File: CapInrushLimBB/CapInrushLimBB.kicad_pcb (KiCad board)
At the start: 2 copper layers, 56.5 x 34.9 mm, 30 parts, among them J1 Screw_Terminal_01x02, J2 Screw_Terminal_01x02, K1 G5LE-1A, Q1 MPSA42, Q2 IRF9540N, Q3 TIP41C, Q4 BSP230 300V 0.21A

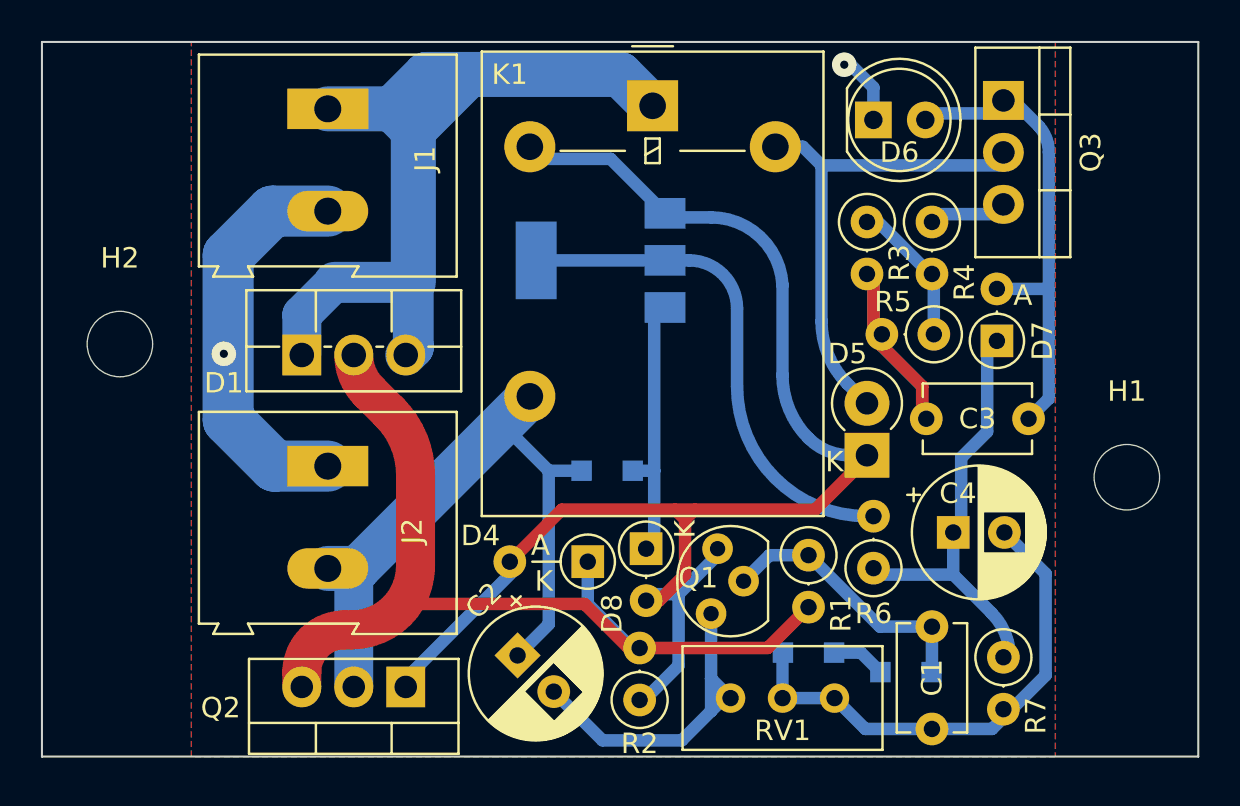
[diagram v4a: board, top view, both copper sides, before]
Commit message: Updated layout and rounded tracks version.
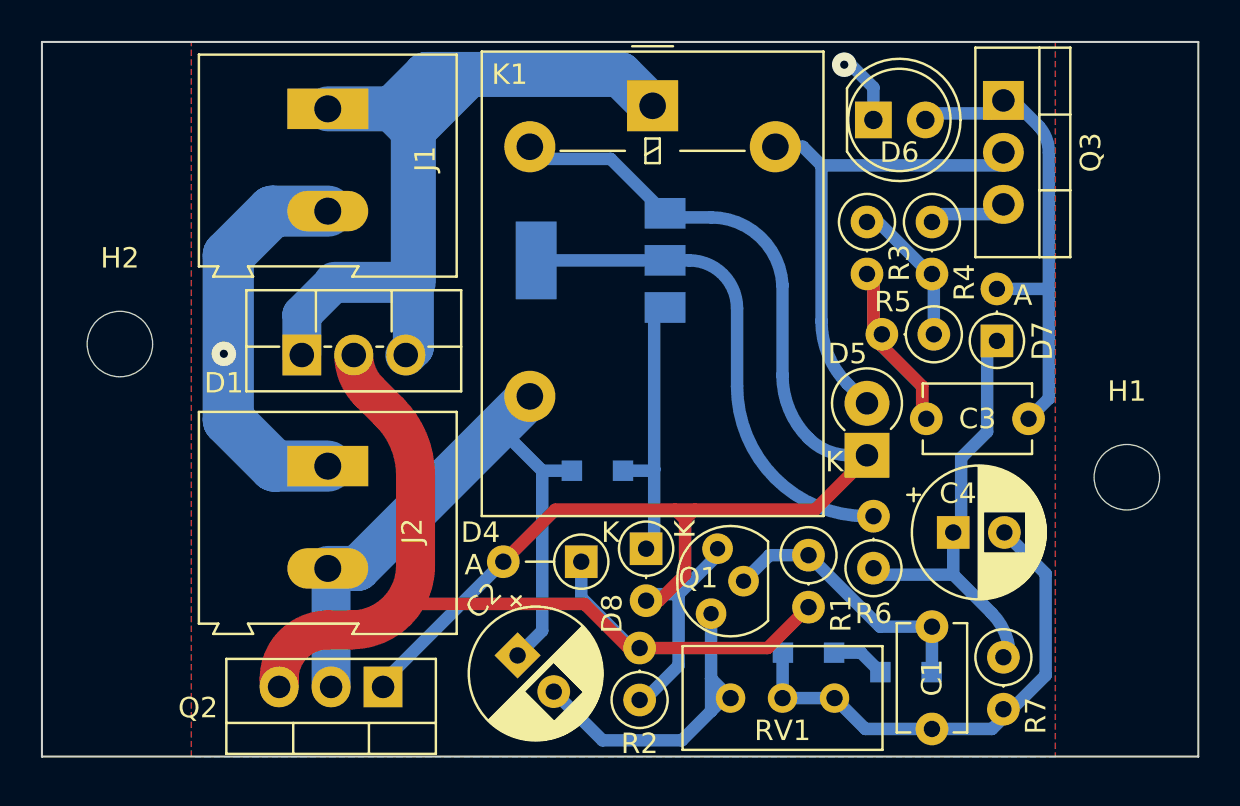
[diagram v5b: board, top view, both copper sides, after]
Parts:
- moved Q2 1.11 mm to (223.7, 156.9)
- moved D9 0.47 mm to (234.2, 146.4)
- moved D4 0.32 mm to (233.4, 150.8)
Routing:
- net /PolProtect: track 47.2 -> 48.3 mm
- net /RLCoilHigh: track 71.0 -> 71.9 mm
- net /RL_Output: track 33.4 -> 32.8 mm
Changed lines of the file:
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@@
   )
   (footprint "Diode_THT:D_DO-35_SOD27_P3.81mm_Vertical_AnodeUp" (layer "F.Cu")
-    (at 233.68613 150.8125 180)
+    (at 233.36863 150.8125 180)
     (descr "Diode, DO-35_SOD27 series, Axial, Vertical, pin pitch=3.81mm, , length*diameter=4*2mm^2, , http://www.diodes.com/_files/packages/DO-35.pdf")
     (tags "Diode DO-35_SOD27 series Axial Vertical pin pitch 3.81mm  length 4mm diameter 2mm")
@@
     (property "Sheetname" "")
     (attr through_hole)
-    (fp_text reference "D4" (at 5.241815 1.27 180) (layer "F.SilkS")
+    (fp_text reference "D4" (at 4.924315 1.42875 180) (layer "F.SilkS")
       (effects (font (size 1 1) (thickness 0.15)))
     )
@@
       (effects (font (size 1 1) (thickness 0.15)))
     )
-    (fp_text user "K" (at 2.144657 -0.9525) (layer "F.SilkS")
-      (effects (font (size 1 1) (thickness 0.15)))
-    )
-    (fp_text user "A" (at 2.31 0.8 180) (layer "F.SilkS")
+    (fp_text user "K" (at -1.425685 1.42875) (layer "F.SilkS")
+      (effects (font (size 1 1) (thickness 0.15)))
+    )
+    (fp_text user "A" (at 5.241815 -0.15875 180) (layer "F.SilkS")
       (effects (font (size 1 1) (thickness 0.15)))
     )
@@
   )
   (footprint "Package_TO_SOT_THT:TO-220-3_Vertical" (layer "F.Cu")
-    (at 224.79 156.9339 180)
+    (at 223.681815 156.9339 180)
     (descr "TO-220-3, Vertical, RM 2.54mm, see https://www.vishay.com/docs/66542/to-220-1.pdf")
     (tags "TO-220-3 Vertical RM 2.54mm")
@@
   )
   (footprint "Diode_SMD:D_SOD-323_HandSoldering" (layer "B.Cu")
-    (at 234.6325 146.3675 180)
+    (at 234.159315 146.3675 180)
     (descr "SOD-323")
     (tags "SOD-323")
@@
   )
   (gr_rect (start 207.01 125.41125) (end 263.525 160.3375) (layer "Edge.Cuts") (width 0.1) (fill none))
-  (segment (start 230.256117 155.394733) (end 231.778065 153.872785) (width 0.6096) (layer "B.Cu") (net 1))
-  (segment (start 231.778065 146.3675) (end 229.555565 144.145) (width 0.6096) (layer "B.Cu") (net 1))
+  (segment (start 221.141815 156.9339) (end 221.141815 151.13) (width 1.905) (layer "B.Cu") (net 1))
   (segment (start 222.445 151.1425) (end 230.855 142.7325) (width 2.2) (layer "B.Cu") (net 1))
-  (segment (start 231.778065 146.3675) (end 233.3825 146.3675) (width 0.6096) (layer "B.Cu") (net 1))
-  (segment (start 231.778065 153.872785) (end 231.778065 146.3675) (width 0.6096) (layer "B.Cu") (net 1))
+  (segment (start 230.256117 155.394733) (end 231.460565 154.190285) (width 0.6096) (layer "B.Cu") (net 1))
   (segment (start 220.98 151.1425) (end 222.445 151.1425) (width 2.2) (layer "B.Cu") (net 1))
-  (segment (start 222.25 156.9339) (end 222.25 151.3375) (width 1.905) (layer "B.Cu") (net 1))
+  (segment (start 232.909315 146.3675) (end 231.460565 146.3675) (width 0.6096) (layer "B.Cu") (net 1))
+  (segment (start 231.460565 146.3675) (end 229.555565 144.4625) (width 0.6096) (layer "B.Cu") (net 1))
+  (segment (start 231.460565 154.190285) (end 231.460565 146.3675) (width 0.6096) (layer "B.Cu") (net 1))
   (segment (start 247.9675 153.9875) (end 244.475 150.495) (width 0.6096) (layer "B.Cu") (net 2))
   (segment (start 250.5075 153.9875) (end 250.5075 156.19) (width 0.6096) (layer "B.Cu") (net 2))
@@
   (segment (start 236.5375 152.7175) (end 237.1725 152.7175) (width 0.6096) (layer "F.Cu") (net 7))
   (segment (start 238.91875 148.2725) (end 238.4425 148.74875) (width 0.6096) (layer "F.Cu") (net 7))
-  (segment (start 237.96086 148.2725) (end 232.41613 148.2725) (width 0.6096) (layer "F.Cu") (net 7))
   (segment (start 237.96086 148.2725) (end 238.91875 148.2725) (width 0.6096) (layer "F.Cu") (net 7))
   (segment (start 244.7925 148.2725) (end 247.3325 145.7325) (width 0.6096) (layer "F.Cu") (net 7))
-  (segment (start 232.41613 148.2725) (end 229.87613 150.8125) (width 0.6096) (layer "F.Cu") (net 7))
   (segment (start 238.4425 151.4475) (end 238.4425 148.74875) (width 0.6096) (layer "F.Cu") (net 7))
   (segment (start 238.91875 148.2725) (end 244.7925 148.2725) (width 0.6096) (layer "F.Cu") (net 7))
+  (segment (start 232.09863 148.2725) (end 229.55863 150.8125) (width 0.6096) (layer "F.Cu") (net 7))
   (segment (start 237.1725 152.7175) (end 238.4425 151.4475) (width 0.6096) (layer "F.Cu") (net 7))
   (segment (start 238.4425 148.74875) (end 237.96086 148.2725) (width 0.6096) (layer "F.Cu") (net 7))
+  (segment (start 237.96086 148.2725) (end 232.09863 148.2725) (width 0.6096) (layer "F.Cu") (net 7))
   (segment (start 236.5375 157.7975) (end 236.22 157.7975) (width 0.6096) (layer "B.Cu") (net 7))
   (segment (start 237.465 133.7875) (end 234.805 131.1275) (width 0.6096) (layer "B.Cu") (net 7))
@@
   (segment (start 246.486604 145.613234) (end 247.3325 145.613234) (width 0.6096) (layer "B.Cu") (net 7))
   (segment (start 237.465 133.7875) (end 237.6625 133.985) (width 0.6096) (layer "B.Cu") (net 7))
-  (segment (start 224.79 156.9339) (end 224.79 156.530565) (width 0.6096) (layer "B.Cu") (net 7))
+  (segment (start 223.681815 156.689315) (end 229.55863 150.8125) (width 0.6096) (layer "B.Cu") (net 7))
   (segment (start 236.445 157.5725) (end 236.22 157.5725) (width 0.6096) (layer "B.Cu") (net 7))
   (segment (start 238.125 152.4) (end 238.125 155.8925) (width 0.6096) (layer "B.Cu") (net 7))
   (segment (start 236.699315 152.7175) (end 237.016815 152.4) (width 0.6096) (layer "B.Cu") (net 7))
+  (segment (start 223.681815 156.9339) (end 223.681815 156.689315) (width 0.6096) (layer "B.Cu") (net 7))
   (segment (start 236.5375 152.7175) (end 236.699315 152.7175) (width 0.6096) (layer "B.Cu") (net 7))
-  (segment (start 224.79 156.530565) (end 230.190565 151.13) (width 0.6096) (layer "B.Cu") (net 7))
   (segment (start 238.125 155.8925) (end 236.445 157.5725) (width 0.6096) (layer "B.Cu") (net 7))
   (segment (start 243.202816 137.29458) (end 243.202816 141.708677) (width 0.6096) (layer "B.Cu") (net 7))
@@
   (segment (start 254 158.4325) (end 254 158.0225) (width 0.6096) (layer "B.Cu") (net 12))
   (segment (start 236.22 155.0325) (end 235.680565 155.0325) (width 0.6096) (layer "F.Cu") (net 13))
-  (segment (start 222.14879 154.14625) (end 221.776815 154.14625) (width 1.905) (layer "F.Cu") (net 13))
-  (segment (start 219.71 156.9339) (end 219.71 156.213065) (width 1.905) (layer "F.Cu") (net 13))
   (segment (start 233.524315 152.87625) (end 224.793065 152.87625) (width 0.6096) (layer "F.Cu") (net 13))
+  (segment (start 225.269315 146.576051) (end 225.269315 151.025725) (width 1.905) (layer "F.Cu") (net 13))
   (segment (start 242.4775 155.0325) (end 244.475 153.035) (width 0.6096) (layer "F.Cu") (net 13))
+  (segment (start 222.991179 142.501863) (end 223.999315 143.51) (width 1.905) (layer "F.Cu") (net 13))
   (segment (start 235.680565 155.0325) (end 233.524315 152.87625) (width 0.6096) (layer "F.Cu") (net 13))
-  (segment (start 225.269315 151.025725) (end 225.269315 146.576051) (width 1.905) (layer "F.Cu") (net 13))
-  (segment (start 222.991179 142.501863) (end 223.999315 143.51) (width 1.905) (layer "F.Cu") (net 13))
+  (segment (start 222.14879 154.14625) (end 220.983065 154.14625) (width 1.905) (layer "F.Cu") (net 13))
   (segment (start 242.4775 155.0325) (end 236.22 155.0325) (width 0.6096) (layer "F.Cu") (net 13))
-  (arc (start 222.14879 154.14625) (mid 224.355334 153.232269) (end 225.269315 151.025725) (width 1.905) (layer "F.Cu") (net 13))
+  (segment (start 218.601815 156.9339) (end 218.601815 156.5275) (width 1.905) (layer "F.Cu") (net 13))
+  (arc (start 222.25 140.7125) (mid 222.442626 141.680896) (end 222.991179 142.501863) (width 1.905) (layer "F.Cu") (net 13))
+  (arc (start 225.269315 151.025725) (mid 224.355334 153.232269) (end 222.14879 154.14625) (width 1.905) (layer "F.Cu") (net 13))
   (arc (start 223.999315 143.51) (mid 224.939253 144.916716) (end 225.269315 146.576051) (width 1.905) (layer "F.Cu") (net 13))
-  (arc (start 222.25 140.7125) (mid 222.442626 141.680896) (end 222.991179 142.501863) (width 1.905) (layer "F.Cu") (net 13))
-  (arc (start 221.776815 154.14625) (mid 220.315356 154.751606) (end 219.71 156.213065) (width 1.905) (layer "F.Cu") (net 13))
-  (segment (start 235.839315 155.0325) (end 233.68613 152.879315) (width 0.6096) (layer "B.Cu") (net 13))
-  (segment (start 233.68613 152.879315) (end 233.68613 150.8125) (width 0.6096) (layer "B.Cu") (net 13))
+  (arc (start 220.983065 154.14625) (mid 219.299267 154.843702) (end 218.601815 156.5275) (width 1.905) (layer "F.Cu") (net 13))
+  (segment (start 233.36863 152.561815) (end 233.36863 150.8125) (width 0.6096) (layer "B.Cu") (net 13))
+  (segment (start 235.839315 155.0325) (end 233.36863 152.561815) (width 0.6096) (layer "B.Cu") (net 13))
   (segment (start 236.22 155.0325) (end 235.839315 155.0325) (width 0.6096) (layer "B.Cu") (net 13))
-  (segment (start 235.8625 146.3675) (end 236.932842 146.3675) (width 0.6096) (layer "B.Cu") (net 14))
-  (segment (start 236.932842 146.3675) (end 236.932842 149.782158) (width 0.6096) (layer "B.Cu") (net 14))
-  (segment (start 236.932842 149.782158) (end 236.5375 150.1775) (width 0.6096) (layer "B.Cu") (net 14))
-  (segment (start 236.932842 146.3675) (end 236.932842 138.3875) (width 0.6096) (layer "B.Cu") (net 14))
+  (segment (start 236.932842 146.292723) (end 236.932842 138.3875) (width 0.6096) (layer "B.Cu") (net 14))
+  (segment (start 236.5375 150.1775) (end 236.932842 149.782158) (width 0.6096) (layer "B.Cu") (net 14))
+  (segment (start 235.409315 146.3675) (end 236.858065 146.3675) (width 0.6096) (layer "B.Cu") (net 14))
+  (segment (start 236.858065 146.3675) (end 236.932842 146.292723) (width 0.6096) (layer "B.Cu") (net 14))
+  (segment (start 236.932842 149.782158) (end 236.932842 146.292723) (width 0.6096) (layer "B.Cu") (net 14))
   (segment (start 250.6 136.8425) (end 250.5075 136.75) (width 0.6096) (layer "B.Cu") (net 15))
   (segment (start 250.6 139.7) (end 250.6 136.8425) (width 0.6096) (layer "B.Cu") (net 15))

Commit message: Changed the reference type, changed current set resistor strategy and updated PCB.
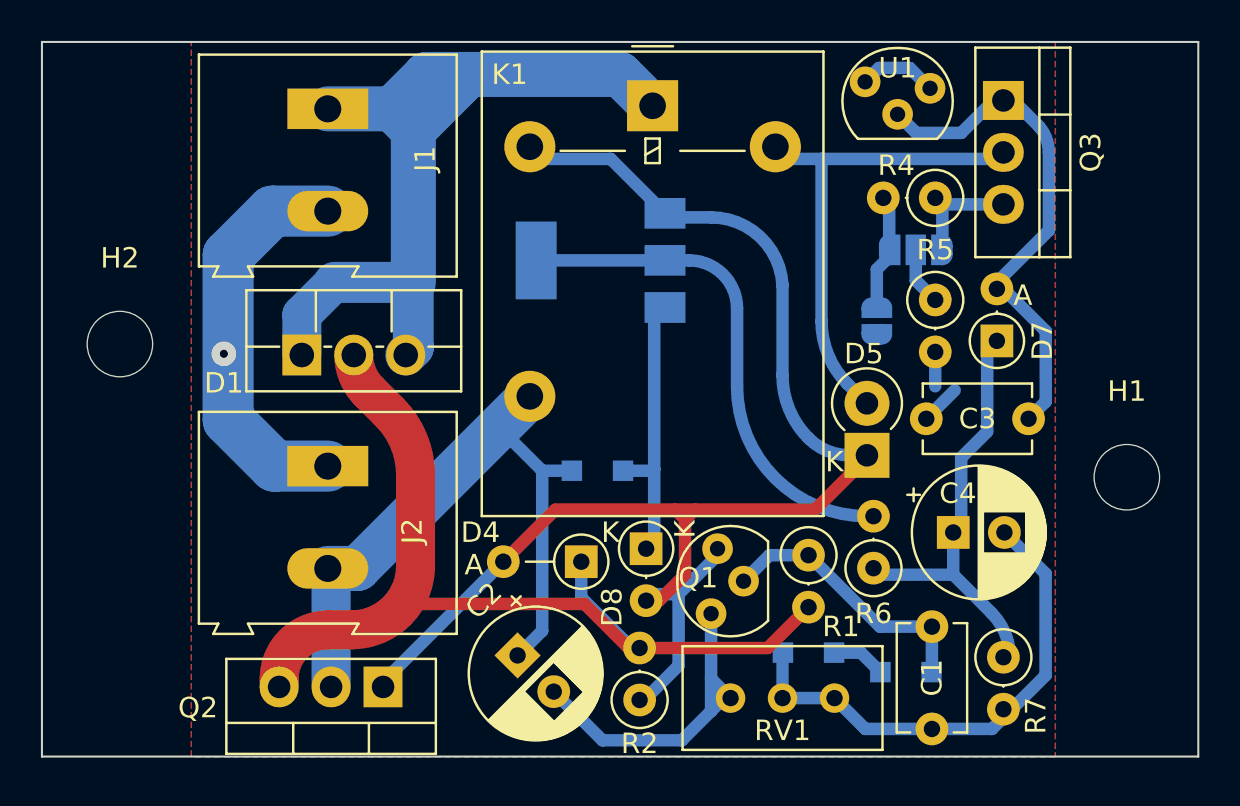
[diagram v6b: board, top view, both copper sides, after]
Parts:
- removed D6: Red LED, LED_THT:LED_D5.0mm
- removed R3: 220R, Resistor_THT:R_Axial_DIN0207_L6.3mm_D2.5mm_P2.54mm_Vertical
- added JP1: SolderJumper_3_Open, Jumper:SolderJumper-3_P1.3mm_Open_RoundedPad1.0x1.5mm, B.Cu at (249.7, 135.6)
- added JP2: SolderJumper_2_Open, Jumper:SolderJumper-2_P1.3mm_Open_RoundedPad1.0x1.5mm, B.Cu at (247.8, 139.1)
- added U1: LM385Z-ADJ, CapInrushLim:TO-92_Inline, F.Cu at (247.6, 128.3)
- R4: value 0R -> 47
- R5: value 110R -> 47
- moved R5 1.68 mm to (250.7, 138.0), turned to -90 degrees
- moved R4 1.19 mm to (250.7, 133.0), turned to 180 degrees
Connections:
- R4 pad 2: Net-(R3-Pad1) -> Net-(JP1-Pad1)
- R5 pad 1: Net-(R3-Pad1) -> Net-(JP1-Pad2)
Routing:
- net /Gnd: track 63.4 -> 52.0 mm, vias 2 -> 1
- net Net-(R3-Pad1): track 6.99 -> 0.00 mm
- net Net-(JP1-Pad1): track 0.00 -> 5.32 mm
- net Net-(JP1-Pad2): track 0.00 -> 2.84 mm
- net Net-(JP1-Pad3): track 3.50 -> 6.15 mm
- net Net-(C3-Pad2): track 22.7 -> 24.6 mm

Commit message: Relayed out relay timer/regulator section to reduce track lengths.
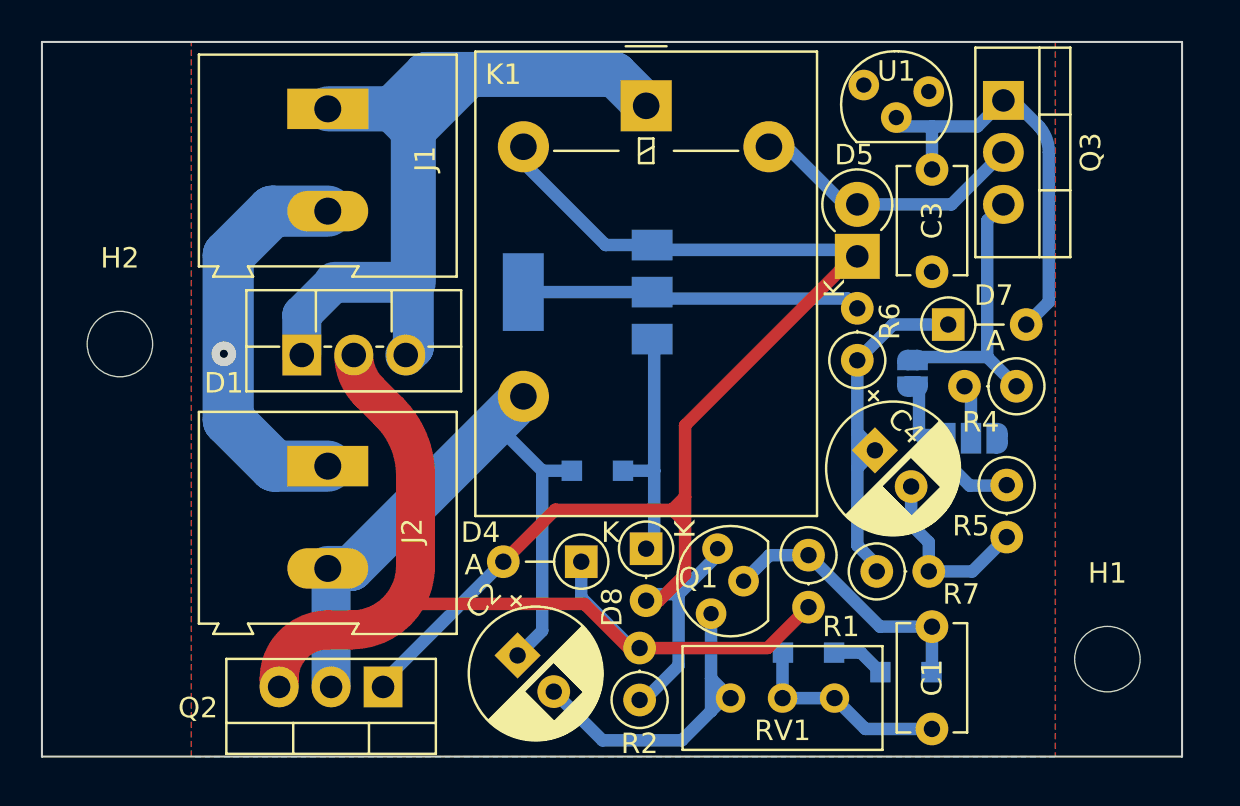
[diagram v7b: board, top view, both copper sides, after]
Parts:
- D7: footprint Diode_THT:D_DO-35_SOD27_P2.54mm_Vertical_AnodeUp -> Diode_THT:D_DO-35_SOD27_P3.81mm_Vertical_AnodeUp
- moved R6 10.2 mm to (246.9, 141.0)
- moved R4 10.0 mm to (254.6, 142.2)
- moved D5 9.73 mm to (246.9, 135.9)
- moved R5 9.70 mm to (254.2, 147.1)
- moved JP1 9.59 mm to (252.4, 144.8)
- moved H1 8.94 mm to (259.1, 155.6)
- moved R7 7.48 mm to (247.8, 151.3), turned to 0 degrees
- moved C3 7.19 mm to (250.5, 136.6), turned to 90 degrees
- moved C4 5.54 mm to (247.7, 145.4), turned to -45 degrees
- moved JP2 3.09 mm to (249.6, 141.6), turned to -90 degrees
- moved D7 2.51 mm to (251.3, 139.2), turned to 0 degrees
- moved Q4 1.67 mm to (233.7, 137.6)
- moved K1 0.31 mm to (236.5, 128.5)
- moved U1 0.17 mm to (247.5, 128.5)
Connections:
- JP1 pad 3: Net-(JP1-Pad3) -> /Gnd
- JP2 pad 1: /Gnd -> Net-(JP2-Pad1)
- Q3 pad 3: Net-(JP1-Pad3) -> Net-(JP2-Pad1)
- R4 pad 1: Net-(JP1-Pad3) -> Net-(JP2-Pad1)
- R4 pad 2: Net-(JP1-Pad1) -> Net-(JP1-Pad2)
- R5 pad 1: Net-(JP1-Pad2) -> Net-(JP1-Pad1)
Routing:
- net Net-(JP2-Pad1): track 0.00 -> 13.5 mm
- net /Gnd: track 52.0 -> 38.8 mm
- net /RLCoilLow: track 24.2 -> 12.4 mm
- net Net-(Q4-Pad2): track 24.6 -> 16.0 mm
- net Net-(JP1-Pad3): track 6.15 -> 0.00 mm
- net Net-(C3-Pad2): track 24.6 -> 19.9 mm
- net Net-(JP1-Pad1): track 5.32 -> 9.70 mm
- net Net-(C4-Pad1): track 21.2 -> 18.3 mm
- net /RLCoilHigh: track 71.9 -> 69.8 mm
- net Net-(D8-Pad1): track 13.5 -> 12.2 mm
- net /RL_Output: track 32.8 -> 32.3 mm
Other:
- board size 56.5 x 34.9 mm -> 55.7 x 34.9 mm
